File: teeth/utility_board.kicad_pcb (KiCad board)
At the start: 2 copper layers, 100 x 100 mm, 49 parts

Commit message: Finish up utility board.
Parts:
- removed D4: BAV70, BAV70 SOT23
- removed D7: , SOT-23
- removed D9: , D_MMBD4148PLM
- removed the J1 at (110.6, 150.0)
- removed the J2 at (110.6, 117.0)
- removed the J3 at (189.4, 117.0)
- removed S10, S2, S4, S6, S8: , CPG1316S01D02_mikeholscher
- removed XX1, XX10, XX11, XX12, XX13, XX14, XX15, XX16, XX2, XX3, XX4, XX5, XX6, XX7, XX8, XX9: mousebites 2mm, mousebites_25mm
- removed XX20, XX23: , 5diode_Breakout_Holes
- removed the XX21 at (193.0, 165.0)
- added ?: , , F.Cu at (173.2, 154.4)
- added ?: , , F.Cu at (176.6, 154.3)
- added ?: , , F.Cu at (176.0, 156.7)
- added ?: , , F.Cu at (106.7, 139.7)
- added ?: , , F.Cu at (181.7, 156.7)
- added ?: , , F.Cu at (119.4, 147.5)
- added ?: , , F.Cu at (106.7, 154.8)
- added ?: , , F.Cu at (120.2, 155.4)
- added ? (x2): , , F.Cu at (120.2, 139.9)
- added ?: , , F.Cu at (102.1, 140.4)
- added ?: , , F.Cu at (173.2, 156.7)
- added ? (x2): , , F.Cu at (123.2, 140.0)
- added ?: , , F.Cu at (116.1, 150.4)
- added ?: , , F.Cu at (111.7, 154.8)
- added ?: , , F.Cu at (116.1, 147.4)
- added ?: , , F.Cu at (116.1, 154.4)
- added ?: , , F.Cu at (111.7, 139.7)
- added ?: , , F.Cu at (102.6, 143.6)
- added ?: , , F.Cu at (103.6, 147.4)
- added ?: , , F.Cu at (102.6, 151.1)
- added ?: , , F.Cu at (102.1, 154.4)
- added ?: , , F.Cu at (178.8, 156.7)
- added ?: , , F.Cu at (109.2, 154.8)
- added ?: , , F.Cu at (123.1, 155.5)
- added ?: , , F.Cu at (103.6, 145.4)
- added ?: , , F.Cu at (116.1, 144.4)
- added ?: , , F.Cu at (103.6, 149.4)
- added C1: 10μF, Capacitor_SMD:C_0603_1608Metric, F.Cu at (177.1, 151.7)
- added C2: 10μF, Capacitor_SMD:C_0603_1608Metric, F.Cu at (175.4, 149.0)
- added CONN1: Battery Connector, Molex_Pico_EZMate_Plus_1x02, F.Cu at (121.7, 151.5)
- added CONN1: Battery Connector, Molex_Pico_EZMate_Plus_1x02, F.Cu at (121.7, 143.8)
- added FID3: FIDUCIAL_1MM, Adafruit ANO Rotary Encoder Breakout:FIDUCIAL_1MM, F.Cu at (131.1, 144.5)
- added FID4: FIDUCIAL_1MM, Adafruit ANO Rotary Encoder Breakout:FIDUCIAL_1MM, F.Cu at (164.1, 168.5)
- added J1: , xiao_plus_cutout, F.Cu at (110.6, 169.6)
- added J1: Conn_01x01_Pin, CKW12:my_mount_hole_M2_pad, F.Cu at (102.1, 154.4)
- added J2: Conn_01x01_Pin, CKW12:my_mount_hole_M2_pad, F.Cu at (102.1, 140.4)
- added J2: , xiao_plus_cutout, F.Cu at (110.6, 117.0)
- added J3: , xiao_plus_cutout, F.Cu at (189.4, 117.0)
- added J3: Conn_01x01_Pin, CKW12:my_mount_hole_M2_pad, F.Cu at (116.1, 140.4)
- added J4: Conn_01x01_Pin, CKW12:my_mount_hole_M2_pad, F.Cu at (116.1, 154.4)
- added JP3: , Adafruit ANO Rotary Encoder Breakout:1X09_ROUND_70, F.Cu at (147.5, 174.8)
- added JST1: , ceoloide:battery_connector_jst_ph_2, F.Cu at (138.8, 122.7)
- added JST1: , ceoloide:battery_connector_jst_ph_2, F.Cu at (124.6, 119.2)
- added JST1: , ceoloide:battery_connector_jst_ph_2, F.Cu at (177.0, 103.7)
- added L1: 2.2μH, huntercook:L_CJIANG_FTC404030S_4.1x4.1x3.0_SMD, F.Cu at (180.2, 152.5)
- added R1: 470kΩ, Resistor_SMD:R_0603_1608Metric, F.Cu at (177.6, 148.2)
- added R2: 51kΩ, Resistor_SMD:R_0603_1608Metric, F.Cu at (175.4, 147.5)
- added REF**: mousebites 2mm, mousebites_25mm, F.Cu at (197.6, 160.0)
- added REF**: mousebites 2mm, mousebites_25mm, F.Cu at (152.7, 180.7)
- added REF**: mousebites 2mm, mousebites_25mm, F.Cu at (124.8, 162.5)
- added REF**: mousebites 2mm, mousebites_25mm, F.Cu at (124.8, 140.7)
- added REF**: mousebites 2mm, mousebites_25mm, F.Cu at (170.3, 137.0)
- added REF**: mousebites 2mm, mousebites_25mm, F.Cu at (110.9, 156.7)
- added REF**: mousebites 2mm, mousebites_25mm, F.Cu at (185.3, 165.0)
- added REF**: mousebites 2mm, mousebites_25mm, F.Cu at (184.6, 147.0)
- added REF**: SOT-323, Package_TO_SOT_SMD:SOT-323_SC-70, F.Cu at (194.2, 138.4)
- added REF**: mousebites 2mm, mousebites_25mm, F.Cu at (170.2, 177.8)
- added REF**: mousebites 2mm, mousebites_25mm, F.Cu at (184.6, 155.0)
- added REF**: mousebites 2mm, mousebites_25mm, F.Cu at (187.8, 153.8)
- added REF**: mousebites 2mm, mousebites_25mm, F.Cu at (118.5, 147.5)
- added REF**: SOT-323, Package_TO_SOT_SMD:SOT-323_SC-70, F.Cu at (177.8, 175.6)
- added REF**: SC-74A-5, Package_TO_SOT_SMD:SC-74A-5_1.55x2.9mm_P0.95mm, F.Cu at (177.5, 164.9)
- added REF**: mousebites 2mm, mousebites_25mm, F.Cu at (185.3, 195.0)
- added REF**: mousebites 2mm, mousebites_25mm, F.Cu at (187.8, 148.2)
- added REF**: mousebites 2mm, mousebites_25mm, F.Cu at (169.9, 131.6)
- added REF**: mousebites 2mm, mousebites_25mm, F.Cu at (185.3, 185.0)
- added REF**: mousebites 2mm, mousebites_25mm, F.Cu at (170.2, 157.0)
- added REF**: mousebites 2mm, mousebites_25mm, F.Cu at (137.4, 134.1)
- added REF**: mousebites 2mm, mousebites_25mm, F.Cu at (185.3, 175.0)
- added REF**: SC-74A-5, Package_TO_SOT_SMD:SC-74A-5_1.55x2.9mm_P0.95mm, F.Cu at (178.8, 139.9)
- added REF**: SOT-363, Package_TO_SOT_SMD:SOT-363_SC-70-6, F.Cu at (192.9, 165.0)
- added REF**: mousebites 2mm, mousebites_25mm, F.Cu at (172.8, 169.9)
- added REF**: mousebites 2mm, mousebites_25mm, F.Cu at (187.8, 139.0)
- added REF**: mousebites 2mm, mousebites_25mm, F.Cu at (182.6, 180.5)
- added REF**: mousebites 2mm, mousebites_25mm, F.Cu at (122.1, 147.5)
- added REF**: mousebites 2mm, mousebites_25mm, F.Cu at (134.8, 102.4)
- added REF**: mousebites 2mm, mousebites_25mm, F.Cu at (169.9, 102.4)
- added REF**: mousebites 2mm, mousebites_25mm, F.Cu at (134.8, 131.6)
- added REF**: mousebites 2mm, mousebites_25mm, F.Cu at (197.6, 134.1)
- added U$25: MOUNTINGHOLE2.5, Adafruit ANO Rotary Encoder Breakout:MOUNTINGHOLE_2.5_PLATED, F.Cu at (162.7, 171.7)
- added U$27: MOUNTINGHOLE2.5, Adafruit ANO Rotary Encoder Breakout:MOUNTINGHOLE_2.5_PLATED, F.Cu at (132.2, 171.7)
- added U$29: MOUNTINGHOLE2.5, Adafruit ANO Rotary Encoder Breakout:MOUNTINGHOLE_2.5_PLATED, F.Cu at (162.7, 141.2)
- added U$30: MOUNTINGHOLE2.5, Adafruit ANO Rotary Encoder Breakout:MOUNTINGHOLE_2.5_PLATED, F.Cu at (132.2, 141.2)
- added U$32: , Adafruit ANO Rotary Encoder Breakout:ADAFRUIT_3.5MM, F.Cu at (137.3, 143.1)
- added U$33: , Adafruit ANO Rotary Encoder Breakout:PCBFEAT-REV-040, F.Cu at (158.0, 150.1)
- added U1: TLV61070ADBV, Package_TO_SOT_SMD:SOT-23-6, F.Cu at (180.4, 148.4)
- added U2: SN74LV1T126DBVR, Package_TO_SOT_SMD:SOT-23-5, F.Cu at (174.3, 151.5)
- added X1: ENCODER_ANO, Adafruit ANO Rotary Encoder Breakout:ENCODER_ANO, B.Cu at (147.5, 156.4)
- added XX18: , 5diode_Breakout_Holes, F.Cu at (192.8, 165.3)
- added XX19: , 5diode_Breakout_Holes, F.Cu at (177.5, 164.9)
- added XX19: , 5diode_Breakout_Holes, F.Cu at (178.8, 139.9)
- added XX21: , 5diode_Breakout_Holes, F.Cu at (178.0, 175.8)
- added XX21: , 5diode_Breakout_Holes, F.Cu at (194.0, 138.2)
- added XX21: , 5diode_Breakout_Holes, F.Cu at (194.1, 155.3)
- S1, S3, S5, S7, S9: footprint CPG1316S01D02_mikeholscher -> HLC_Custom:PG1316S_Square_Pads
- moved D5 9.74 mm to (194.1, 155.3)
- moved D8 0.97 mm to (143.0, 187.6)
- moved S5 0.97 mm to (143.0, 190.1)
- moved S7 0.97 mm to (159.0, 190.1)
- moved S9 0.97 mm to (175.0, 190.1)
- moved S1 0.97 mm to (111.0, 190.1)
- moved S3 0.97 mm to (127.0, 190.1)
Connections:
- D8 pad 1: index_home -> inner_home
- D8 pad 3: ring_home -> pinky_home
- D8 pad 4: inner_home -> index_home
- D8 pad 5: pinky_home -> ring_home
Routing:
- net P1.14: track 0.00 -> 95.7 mm
- net P1.05: track 0.00 -> 76.4 mm
- net (no net): track 0.00 -> 74.7 mm
- net P1.13: track 0.00 -> 58.1 mm, vias 0 -> 2
- net SW2: track 0.00 -> 47.3 mm
- net P0.03: track 0.00 -> 42.5 mm
- net COMB: track 0.00 -> 40.1 mm
- net pinky_home: track 0.00 -> 40.1 mm
- net inner_home: track 0.00 -> 32.4 mm
- net P0.15: track 0.00 -> 31.3 mm
- net Net-(J3-Pin_1): track 0.00 -> 30.8 mm, vias 0 -> 2
- net SW1: track 0.00 -> 30.0 mm
- net ENC_A: track 0.00 -> 29.0 mm
- net SW3: track 0.00 -> 28.2 mm
- net SW5: track 0.00 -> 25.6 mm
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- added copper zone on B.Cu, net GND
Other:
- outline, holes or cut-outs redrawn
- net class Default removed
- board text added: "BAV70"
- board text added: "COMA"
- board text added: "COMB"
- board text added: "ENCA"
- board text added: "ENCB"
- board text added: "MMBD4148PLM-7"
- board text added: "Rotary Navigation Encoder Breakout"
- board text added: "SS109"
- board text added: "SW1"
- board text added: "SW2"
- board text added: "SW3"
- board text added: "SW4"
- board text added: "SW5"

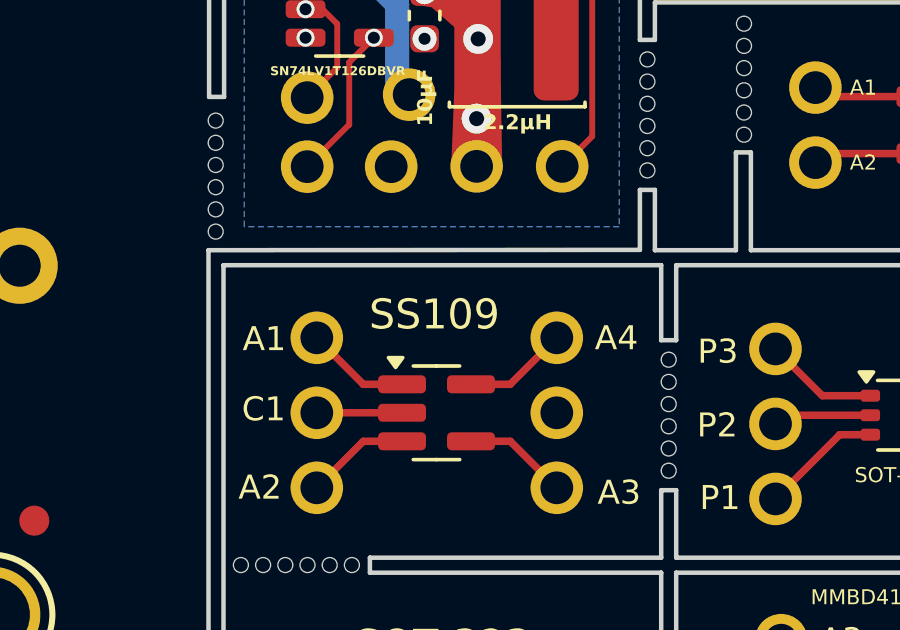
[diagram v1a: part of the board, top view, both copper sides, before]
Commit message: Create new utility board version with 5-way, CKW12, ANO, an cutout-mount nice nano.
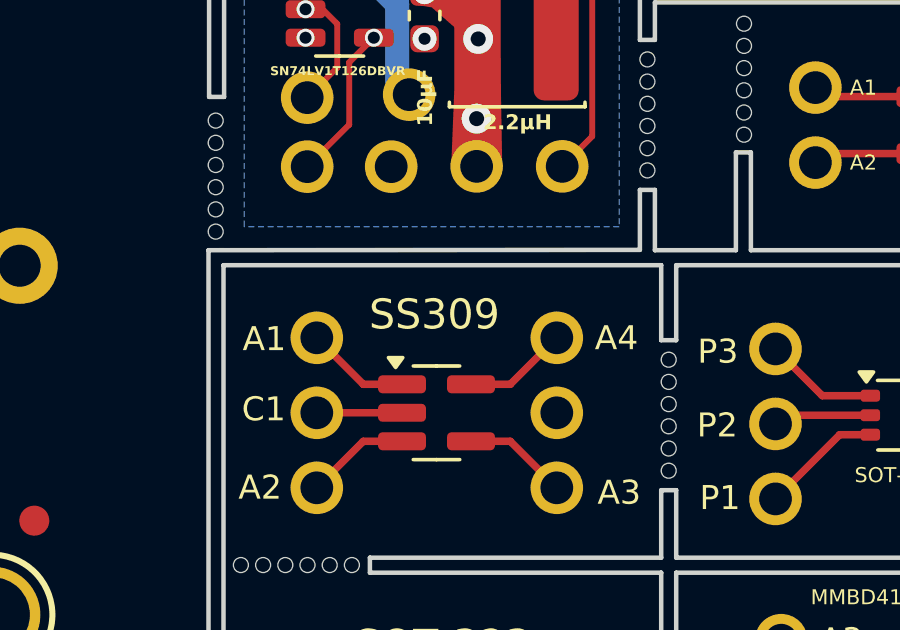
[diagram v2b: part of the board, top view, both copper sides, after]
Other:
- board text added: "SS309"
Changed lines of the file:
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@@
 		)
 	)
-	(gr_text "SS109"
+	(gr_text "SS309"
 		(at 175.26 162.23 0)
 		(layer "F.SilkS")
